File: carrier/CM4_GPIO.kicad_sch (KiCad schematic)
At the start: 19 parts, among them J19 Left GPIO, J20 Right GPIO, J5 System, SW1 SW_DIP_x02, U10 MagJack-A70-112-331N126, U6 74LVC1G07SE-7, U7 TPD4EUSB30, U8 TPD4EUSB30, U9 74LVC1G07SE-7

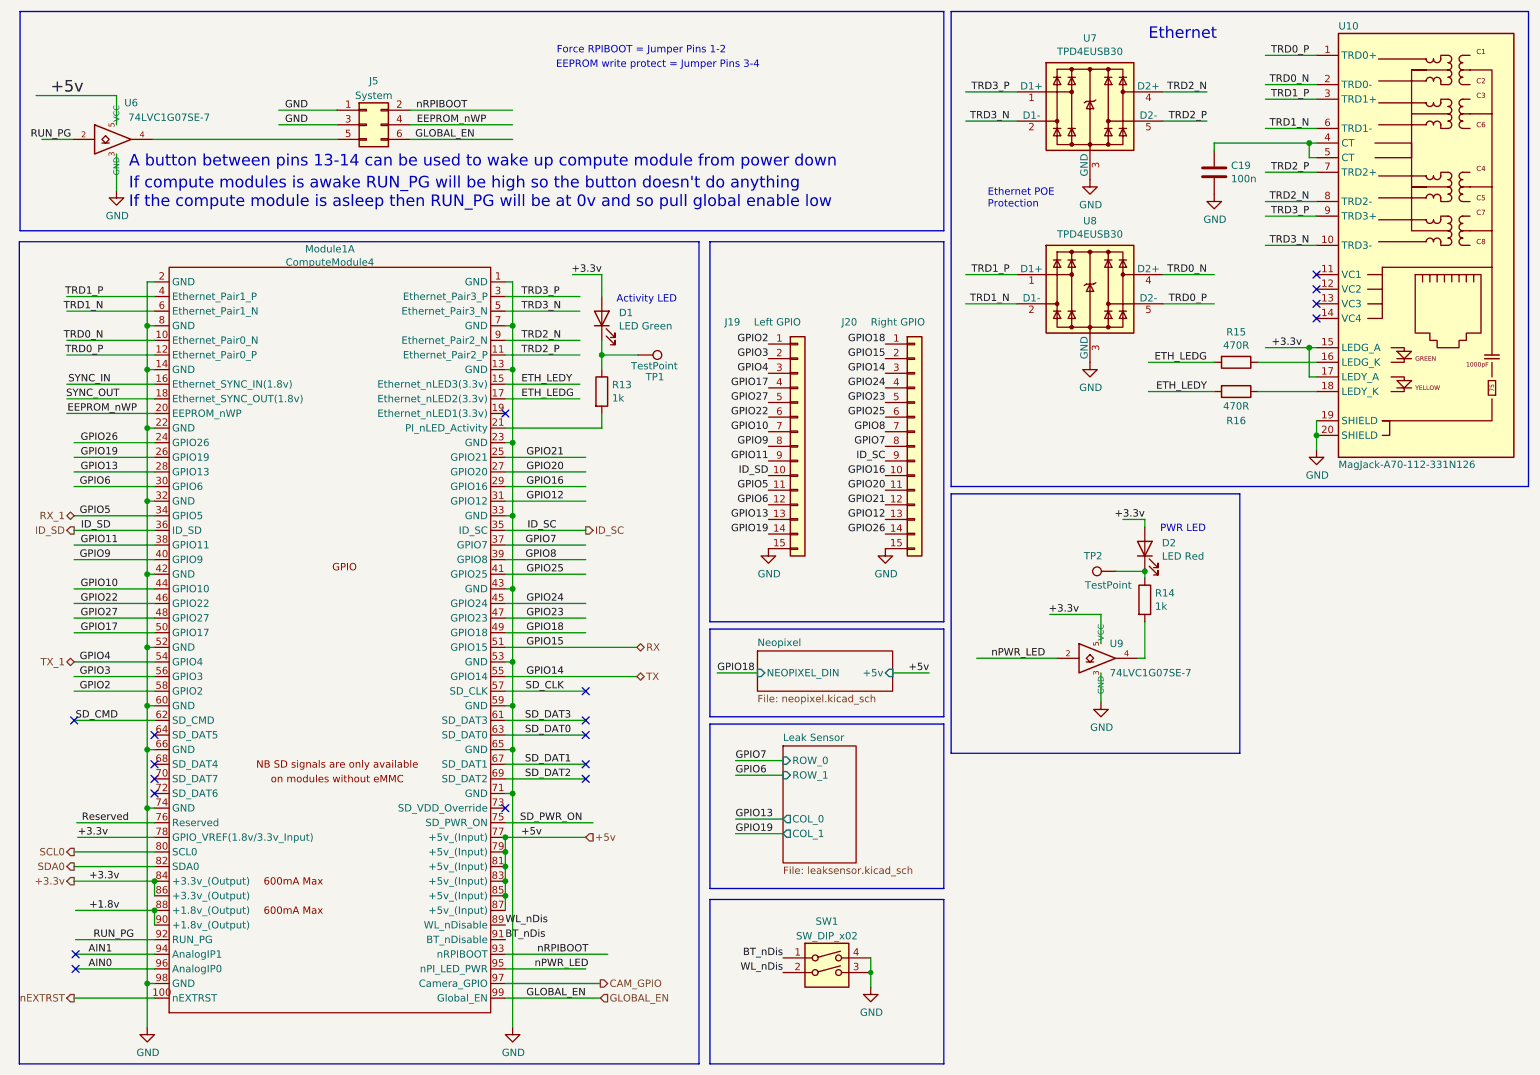
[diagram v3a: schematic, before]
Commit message: Refactor: re-annotated schematic with cm4 connector POS configured
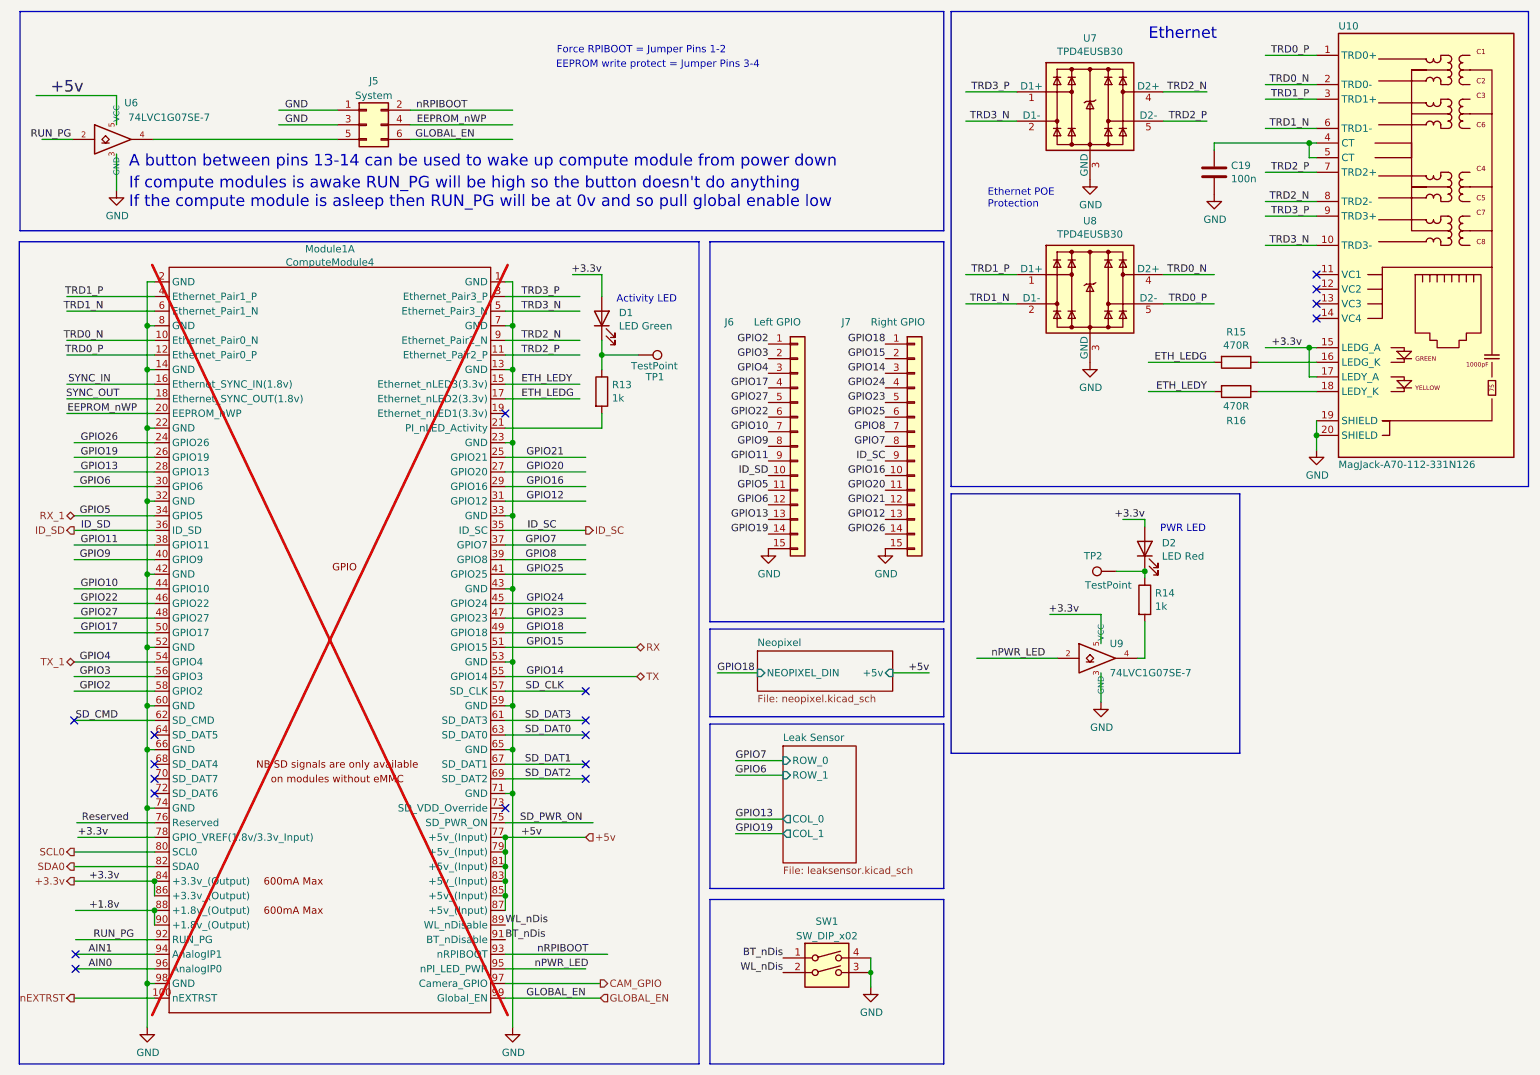
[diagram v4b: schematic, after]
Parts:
- Module1: now not fitted
- renumbered J19 to J6, J20 to J7
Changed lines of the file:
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@@
   (symbol (lib_id "power:GND") (at 99.06 189.865 0) (unit 1)
     (in_bom yes) (on_board yes) (dnp no)
-    (property "Reference" "#PWR035" (at 99.06 196.215 0)
+    (property "Reference" "#PWR036" (at 99.06 196.215 0)
       (effects (font (size 1.27 1.27)) hide)
     )
@@
       (project "carrier"
         (path "/4b1cea9d-93bc-4380-88c3-ede99bb53de2/620225a5-f804-40cd-b5ea-f876279ff075"
-          (reference "#PWR035") (unit 1)
+          (reference "#PWR036") (unit 1)
         )
       )
@@
   (symbol (lib_id "power:GND") (at 199.39 74.295 0) (unit 1)
     (in_bom yes) (on_board yes) (dnp no)
-    (property "Reference" "#PWR039" (at 199.39 80.645 0)
+    (property "Reference" "#PWR041" (at 199.39 80.645 0)
       (effects (font (size 1.27 1.27)) hide)
     )
@@
       (project "carrier"
         (path "/4b1cea9d-93bc-4380-88c3-ede99bb53de2/620225a5-f804-40cd-b5ea-f876279ff075"
-          (reference "#PWR039") (unit 1)
+          (reference "#PWR041") (unit 1)
         )
       )
@@
   (symbol (lib_id "power:GND") (at 220.98 45.085 0) (unit 1)
     (in_bom yes) (on_board yes) (dnp no)
-    (property "Reference" "#PWR041" (at 220.98 51.435 0)
+    (property "Reference" "#PWR043" (at 220.98 51.435 0)
       (effects (font (size 1.27 1.27)) hide)
     )
@@
       (project "carrier"
         (path "/4b1cea9d-93bc-4380-88c3-ede99bb53de2/620225a5-f804-40cd-b5ea-f876279ff075"
-          (reference "#PWR041") (unit 1)
+          (reference "#PWR043") (unit 1)
         )
       )
@@
   (symbol (lib_id "power:GND") (at 143.51 106.68 0) (unit 1)
     (in_bom yes) (on_board yes) (dnp no)
-    (property "Reference" "#PWR078" (at 143.51 113.03 0)
+    (property "Reference" "#PWR037" (at 143.51 113.03 0)
       (effects (font (size 1.27 1.27)) hide)
     )
@@
       (project "carrier"
         (path "/4b1cea9d-93bc-4380-88c3-ede99bb53de2/620225a5-f804-40cd-b5ea-f876279ff075"
-          (reference "#PWR078") (unit 1)
+          (reference "#PWR037") (unit 1)
         )
       )
@@
   (symbol (lib_id "power:GND") (at 161.29 182.88 0) (unit 1)
     (in_bom yes) (on_board yes) (dnp no)
-    (property "Reference" "#PWR036" (at 161.29 189.23 0)
+    (property "Reference" "#PWR038" (at 161.29 189.23 0)
       (effects (font (size 1.27 1.27)) hide)
     )
@@
       (project "carrier"
         (path "/4b1cea9d-93bc-4380-88c3-ede99bb53de2/620225a5-f804-40cd-b5ea-f876279ff075"
-          (reference "#PWR036") (unit 1)
+          (reference "#PWR038") (unit 1)
         )
       )
@@
   (symbol (lib_id "power:GND") (at 238.76 89.535 0) (unit 1)
     (in_bom yes) (on_board yes) (dnp no)
-    (property "Reference" "#PWR042" (at 238.76 95.885 0)
+    (property "Reference" "#PWR044" (at 238.76 95.885 0)
       (effects (font (size 1.27 1.27)) hide)
     )
@@
       (project "carrier"
         (path "/4b1cea9d-93bc-4380-88c3-ede99bb53de2/620225a5-f804-40cd-b5ea-f876279ff075"
-          (reference "#PWR042") (unit 1)
+          (reference "#PWR044") (unit 1)
         )
       )
@@
   (symbol (lib_id "power:GND") (at 199.39 42.545 0) (unit 1)
     (in_bom yes) (on_board yes) (dnp no)
-    (property "Reference" "#PWR038" (at 199.39 48.895 0)
+    (property "Reference" "#PWR040" (at 199.39 48.895 0)
       (effects (font (size 1.27 1.27)) hide)
     )
@@
       (project "carrier"
         (path "/4b1cea9d-93bc-4380-88c3-ede99bb53de2/620225a5-f804-40cd-b5ea-f876279ff075"
-          (reference "#PWR038") (unit 1)
+          (reference "#PWR040") (unit 1)
         )
       )
@@
   (symbol (lib_id "power:GND") (at 35.56 189.865 0) (unit 1)
     (in_bom yes) (on_board yes) (dnp no)
-    (property "Reference" "#PWR034" (at 35.56 196.215 0)
+    (property "Reference" "#PWR035" (at 35.56 196.215 0)
       (effects (font (size 1.27 1.27)) hide)
     )
@@
       (project "carrier"
         (path "/4b1cea9d-93bc-4380-88c3-ede99bb53de2/620225a5-f804-40cd-b5ea-f876279ff075"
-          (reference "#PWR034") (unit 1)
+          (reference "#PWR035") (unit 1)
         )
       )
@@
   (symbol (lib_id "Connector_Generic:Conn_01x15") (at 148.59 88.9 0) (unit 1)
     (in_bom yes) (on_board yes) (dnp no)
-    (property "Reference" "J19" (at 135.89 67.31 0)
+    (property "Reference" "J6" (at 135.89 67.31 0)
       (effects (font (size 1.27 1.27)) (justify left))
     )
@@
       (project "carrier"
         (path "/4b1cea9d-93bc-4380-88c3-ede99bb53de2/620225a5-f804-40cd-b5ea-f876279ff075"
-          (reference "J19") (unit 1)
+          (reference "J6") (unit 1)
         )
       )
@@
   (symbol (lib_id "power:GND") (at 163.83 106.68 0) (unit 1)
     (in_bom yes) (on_board yes) (dnp no)
-    (property "Reference" "#PWR079" (at 163.83 113.03 0)
+    (property "Reference" "#PWR039" (at 163.83 113.03 0)
       (effects (font (size 1.27 1.27)) hide)
     )
@@
       (project "carrier"
         (path "/4b1cea9d-93bc-4380-88c3-ede99bb53de2/620225a5-f804-40cd-b5ea-f876279ff075"
-          (reference "#PWR079") (unit 1)
+          (reference "#PWR039") (unit 1)
         )
       )
@@
   (symbol (lib_id "power:GND") (at 30.226 44.45 0) (unit 1)
     (in_bom yes) (on_board yes) (dnp no)
-    (property "Reference" "#PWR033" (at 30.226 50.8 0)
+    (property "Reference" "#PWR034" (at 30.226 50.8 0)
       (effects (font (size 1.27 1.27)) hide)
     )
@@
       (project "carrier"
         (path "/4b1cea9d-93bc-4380-88c3-ede99bb53de2/620225a5-f804-40cd-b5ea-f876279ff075"
-          (reference "#PWR033") (unit 1)
+          (reference "#PWR034") (unit 1)
         )
       )
@@
   )
   (symbol (lib_id "CM4IO:ComputeModule4-CM4") (at 69.85 116.205 0) (unit 1)
-    (in_bom yes) (on_board yes) (dnp no)
+    (in_bom yes) (on_board yes) (dnp yes)
     (property "Reference" "Module1" (at 67.31 54.61 0)
       (effects (font (size 1.27 1.27)))
@@
   (symbol (lib_id "Connector_Generic:Conn_01x15") (at 168.91 88.9 0) (unit 1)
     (in_bom yes) (on_board yes) (dnp no)
-    (property "Reference" "J20" (at 156.21 67.31 0)
+    (property "Reference" "J7" (at 156.21 67.31 0)
       (effects (font (size 1.27 1.27)) (justify left))
     )
@@
       (project "carrier"
         (path "/4b1cea9d-93bc-4380-88c3-ede99bb53de2/620225a5-f804-40cd-b5ea-f876279ff075"
-          (reference "J20") (unit 1)
+          (reference "J7") (unit 1)
         )
       )
@@
   (symbol (lib_id "power:GND") (at 201.295 133.35 0) (unit 1)
     (in_bom yes) (on_board yes) (dnp no)
-    (property "Reference" "#PWR040" (at 201.295 139.7 0)
+    (property "Reference" "#PWR042" (at 201.295 139.7 0)
       (effects (font (size 1.27 1.27)) hide)
     )
@@
       (project "carrier"
         (path "/4b1cea9d-93bc-4380-88c3-ede99bb53de2/620225a5-f804-40cd-b5ea-f876279ff075"
-          (reference "#PWR040") (unit 1)
-        )
-      )
+          (reference "#PWR042") (unit 1)
+        )
+      )

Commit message: Feat: major revamps to pcb, finished bom and pos
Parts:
- Module1: Field5 2off DF40C-100DS-0.4V -> 2x DF40C-100DS-0.4V
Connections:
- net +3.3v: now also U10.11 (LEDG_A), U10.13 (LEDY_A); no longer U10.15 (LEDG_A), U10.17 (LEDY_A)
- net GND: now also U10.15 (SHIELD), U10.16 (SHIELD); no longer U10.19 (SHIELD), U10.20 (SHIELD)
- net at R16.1: now also U10.14 (LEDY_K); no longer U10.18 (LEDY_K)
- net at U10.12 (LEDG_K): now also R15.1
- no-connect marks 18 -> 14
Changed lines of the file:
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@@
   (no_connect (at 97.79 151.765))
   (no_connect (at 97.79 83.185))
-  (no_connect (at 238.76 61.595))
-  (no_connect (at 238.76 59.055))
   (no_connect (at 23.114 177.165))
   (no_connect (at 36.83 146.685))
@@
   (no_connect (at 111.76 131.445))
   (no_connect (at 36.83 139.065))
-  (no_connect (at 238.76 64.135))
   (no_connect (at 36.83 149.225))
   (no_connect (at 23.114 179.705))
@@
   (no_connect (at 111.76 136.525))
   (no_connect (at 111.76 146.685))
-  (no_connect (at 238.76 66.675))
   (no_connect (at 36.83 144.145))
   (wire (pts (xy 35.56 111.125) (xy 35.56 123.825))
@@
       (effects (font (size 1.27 1.27)) hide)
     )
-    (property "Datasheet" "http://optoelectronics.liteon.com/upload/download/DS22-2000-210/LTST-S270KRKT.pdf" (at 208.915 106.68 0)
+    (property "Datasheet" "~" (at 208.915 106.68 0)
       (effects (font (size 1.27 1.27)) hide)
     )
@@
       (effects (font (size 1.27 1.27)) hide)
     )
-    (property "Datasheet" "https://www.diodes.com/assets/Datasheets/74LVC1G07.pdf" (at 201.295 125.73 0)
+    (property "Datasheet" "http://www.ti.com/lit/sg/scyt129e/scyt129e.pdf" (at 201.295 125.73 0)
       (effects (font (size 1.27 1.27)) hide)
     )
@@
       (effects (font (size 1.27 1.27)) hide)
     )
-    (property "Datasheet" "" (at 203.9112 105.537 0)
+    (property "Datasheet" "~" (at 203.9112 105.537 0)
       (effects (font (size 1.27 1.27)) hide)
     )
@@
       (effects (font (size 1.27 1.27)) hide)
     )
-    (property "Field5" "2off DF40C-100DS-0.4V" (at 69.85 116.205 0)
+    (property "Field5" "2x DF40C-100DS-0.4V" (at 69.85 116.205 0)
       (effects (font (size 1.27 1.27)) hide)
     )
@@
       (effects (font (size 1.27 1.27)) hide)
     )
-    (property "Datasheet" "https://fscdn.rohm.com/en/products/databook/datasheet/passive/resistor/chip_resistor/mcr-e.pdf" (at 224.79 79.375 0)
+    (property "Datasheet" "~" (at 224.79 79.375 0)
       (effects (font (size 1.27 1.27)) hide)
     )
@@
       (effects (font (size 1.27 1.27)) hide)
     )
-    (property "Datasheet" "" (at 120.904 78.105 0)
+    (property "Datasheet" "~" (at 120.904 78.105 0)
       (effects (font (size 1.27 1.27)) hide)
     )
@@
     (pin "15")
     (pin "16")
-    (pin "17")
-    (pin "18")
-    (pin "19")
     (pin "2")
-    (pin "20")
     (pin "3")
     (pin "4")
@@
       (effects (font (size 1.27 1.27)) hide)
     )
-    (property "Datasheet" "http://optoelectronics.liteon.com/upload/download/DS22-2000-226/LTST-S270KGKT.pdf" (at 114.554 66.675 0)
+    (property "Datasheet" "~" (at 114.554 66.675 0)
       (effects (font (size 1.27 1.27)) hide)
     )
@@
       (effects (font (size 1.27 1.27)) hide)
     )
-    (property "Datasheet" "https://fscdn.rohm.com/en/products/databook/datasheet/passive/resistor/chip_resistor/mcr-e.pdf" (at 224.79 74.295 0)
+    (property "Datasheet" "~" (at 224.79 74.295 0)
       (effects (font (size 1.27 1.27)) hide)
     )
@@
       (effects (font (size 1.27 1.27)) hide)
     )
-    (property "Datasheet" "https://www.diodes.com/assets/Datasheets/74LVC1G07.pdf" (at 30.226 35.56 0)
+    (property "Datasheet" "http://www.ti.com/lit/sg/scyt129e/scyt129e.pdf" (at 30.226 35.56 0)
       (effects (font (size 1.27 1.27)) hide)
     )
@@
       (effects (font (size 1.27 1.27)) hide)
     )
-    (property "Datasheet" "https://fscdn.rohm.com/en/products/databook/datasheet/passive/resistor/chip_resistor/mcr-e.pdf" (at 208.915 115.57 0)
+    (property "Datasheet" "~" (at 208.915 115.57 0)
       (effects (font (size 1.27 1.27)) hide)
     )
@@
       (effects (font (size 1.27 1.27)) hide)
     )
-    (property "Datasheet" "https://search.murata.co.jp/Ceramy/image/img/A01X/G101/ENG/GRM155R71C104KA88-01.pdf" (at 220.98 41.275 0)
+    (property "Datasheet" "~" (at 220.98 41.275 0)
       (effects (font (size 1.27 1.27)) hide)
     )
@@
       (effects (font (size 1.27 1.27)) hide)
     )
-    (property "Datasheet" "https://fscdn.rohm.com/en/products/databook/datasheet/passive/resistor/chip_resistor/mcr-e.pdf" (at 114.554 79.375 0)
-      (effects (font (size 1.27 1.27)) hide)
-    )
+    (property "Datasheet" "~" (at 114.554 79.375 0)
+      (effects (font (size 1.27 1.27)) hide)
+    )

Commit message: Feat: tidied up carrier board, added 3d models, fully prepared for production
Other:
- company: MUREX -> MUREX Robotics [Byran Huang]
- title: CM4 GPIO -> Carrier Board
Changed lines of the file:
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@@
   (paper "A4")
   (title_block
-    (title "CM4 GPIO")
-    (company "MUREX")
+    (title "Carrier Board")
+    (date "2023-06-18")
+    (rev "V1.0")
+    (company "MUREX Robotics [Byran Huang]")
+    (comment 1 "//DO IT RIGHT,  DO IT MUREX")
+    (comment 2 "// ATTEMPT THE IMPOSSIBLE")
+    (comment 3 "CM4-based ROV (robotics) control board.")
+    (comment 4 "The MUREX Carrier Board is the world's first open-source ")
   )
   (junction (at 35.56 111.125) (diameter 1.016) (color 0 0 0 0)

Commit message: Feat: fully production ready (?)
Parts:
- U10: value MagJack-A70-112-331N126 -> RB1-2S5BAK1A
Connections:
- net +3.3v: now also U10.L1 (LEDY_A), U10.L4 (LEDG_A); no longer U10.11 (LEDG_A), U10.13 (LEDY_A)
- net TRD1_N: now also U10.4 (TRD1-); no longer U10.6 (TRD1-)
- net at R16.1: now also U10.L2 (LEDY_K); no longer U10.14 (LEDY_K)
- net at R15.1: now also U10.L3 (LEDG_K); no longer U10.12 (LEDG_K)
- net at C19.1, U10.5 (CT): now also U10.6 (CT); no longer U10.4 (CT)
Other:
- moved on the sheet: C19, R15, R16, U10
